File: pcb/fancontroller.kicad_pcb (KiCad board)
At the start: 2 copper layers, 19 x 41.9 mm, 6 parts, among them J1 Thermo

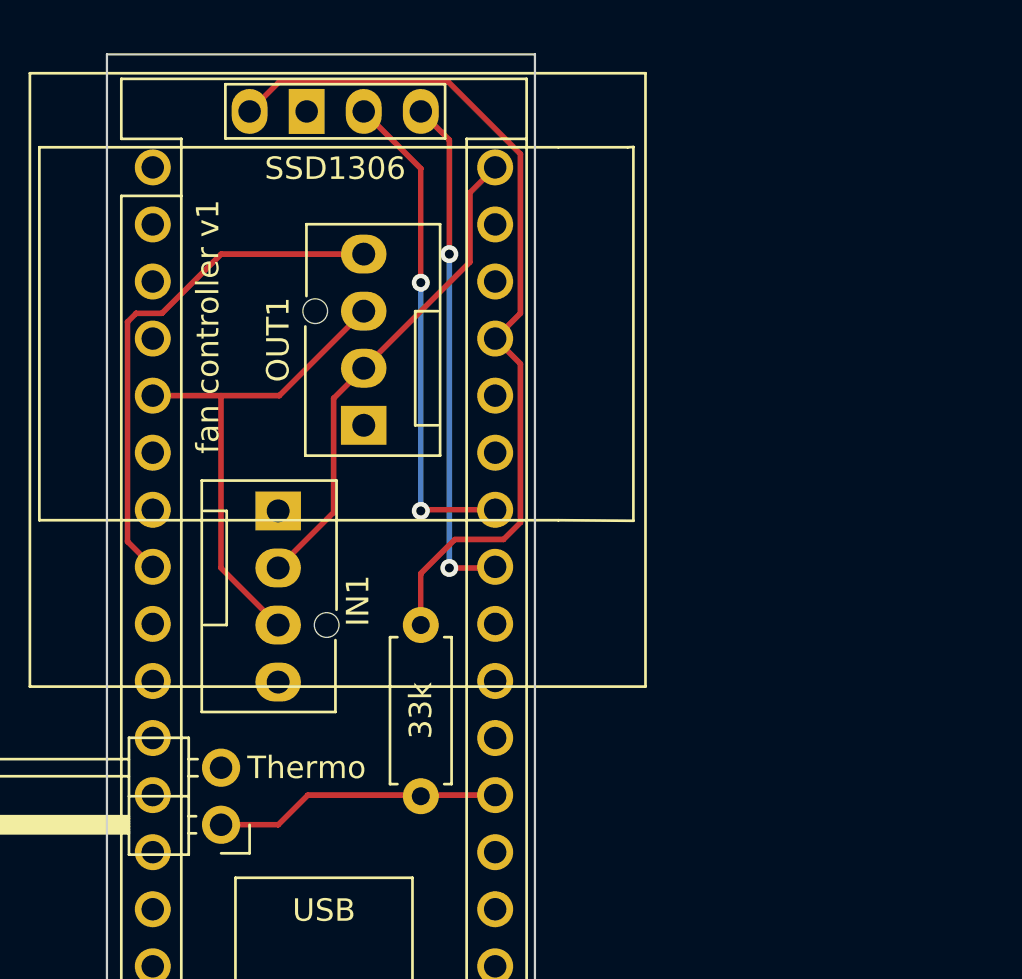
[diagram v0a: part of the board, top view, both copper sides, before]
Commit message: Update to Kicad 8, clean up schematic, add second fan header to schematic
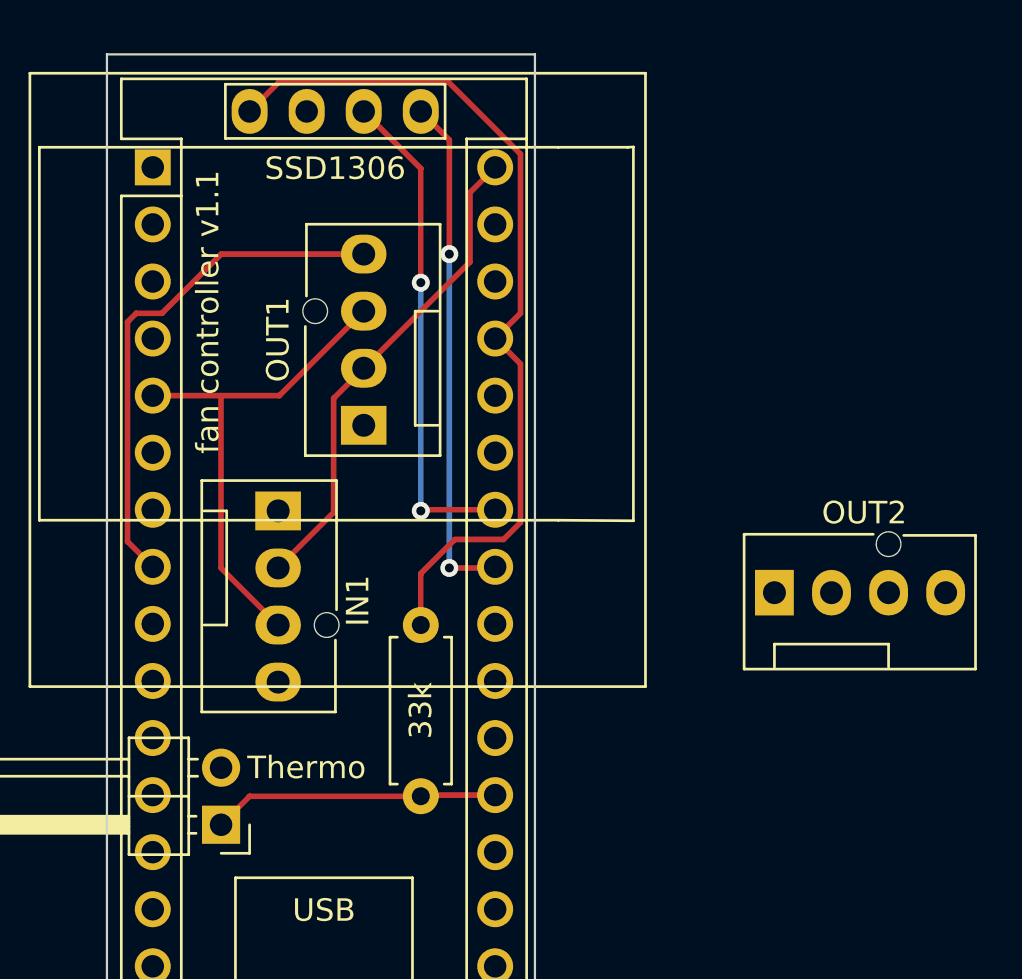
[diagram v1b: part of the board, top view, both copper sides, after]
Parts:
- added OUT2: FAN_HEADER, Connector:FanPinHeader_1x04_P2.54mm_Vertical, F.Cu at (119.9, 90.0)
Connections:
- net Net-(A1-+5V) renamed +5V
- net Net-(A1-A0) renamed /TEMP
- net Net-(A1-A4) renamed /SDA
- net Net-(A1-A5) renamed /SCL
- net Net-(A1-D2) renamed /TACH1
- net Net-(A1-D5) renamed /PWM
- A1 pad 6: unconnected-(A1-D3-Pad6) -> /TACH2
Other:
- board text added: "fan controller v1.1"
- board text removed: "fan controller v1"

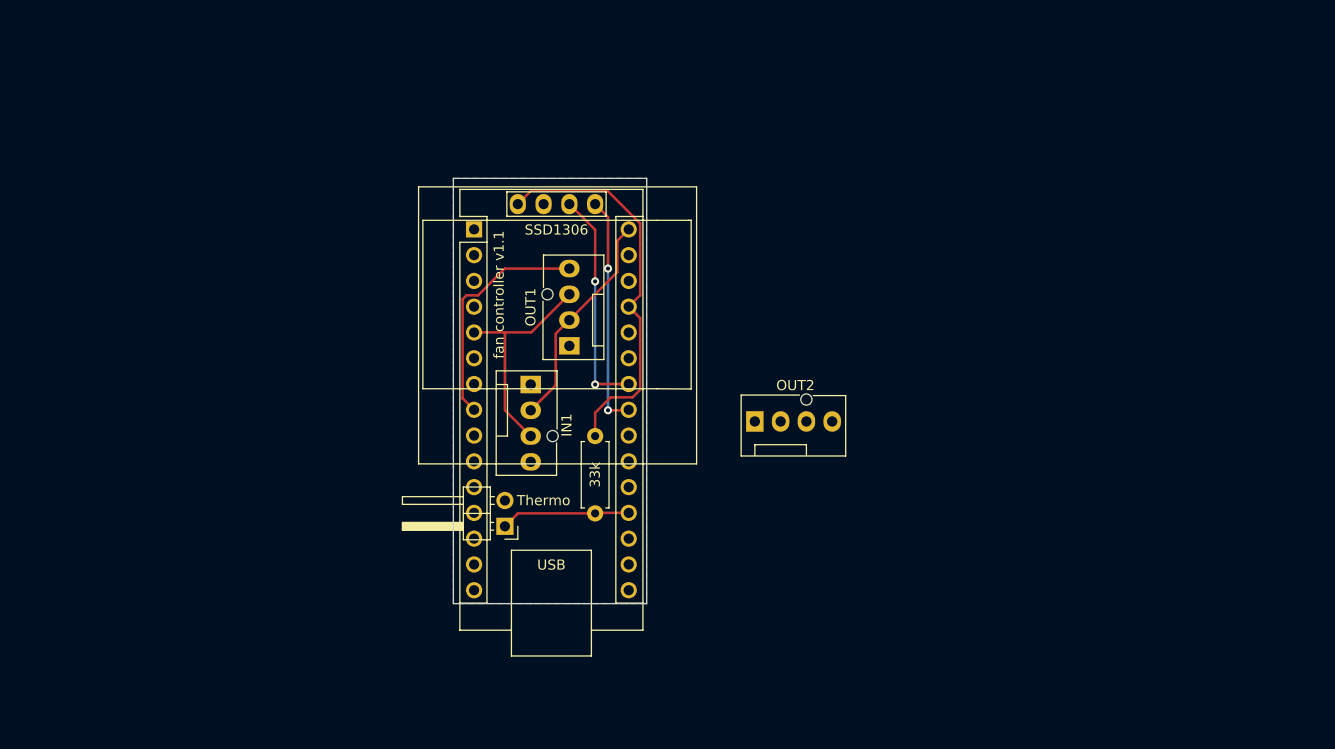
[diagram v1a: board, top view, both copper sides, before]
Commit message: v2: add stm32cubemx config, early draft of pcb layout, update version
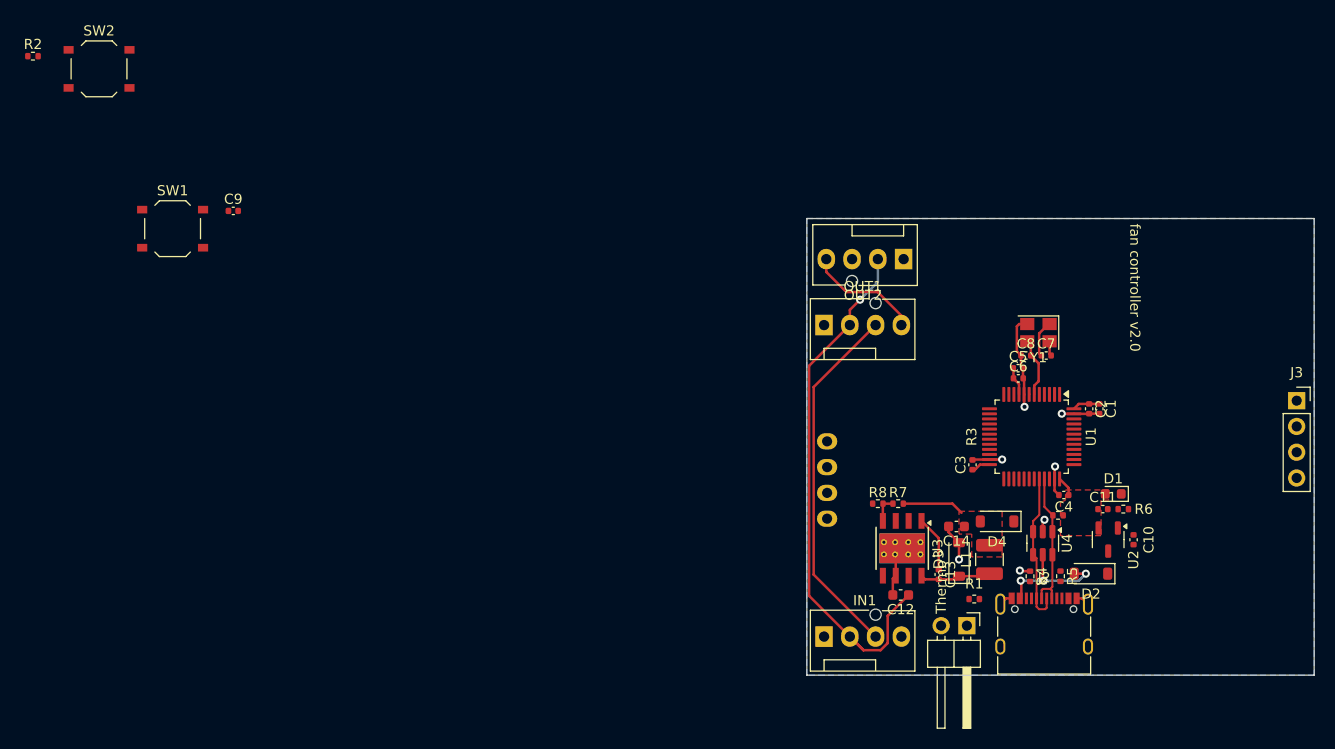
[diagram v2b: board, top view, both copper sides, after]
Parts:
- removed A1: Arduino_Nano_v3.x, Module:Arduino_Nano
- added C1: 4.7uF, Capacitor_SMD:C_0402_1005Metric, F.Cu at (153.8, 88.8)
- added C10: 1uF, Capacitor_SMD:C_0402_1005Metric, F.Cu at (157.2, 101.7)
- added C11: 1uF, Capacitor_SMD:C_0402_1005Metric, F.Cu at (154.2, 98.6)
- added C12: 10uF, Capacitor_SMD:C_0603_1608Metric, F.Cu at (134.2, 107.1)
- added C13: 10nF, Capacitor_SMD:C_0402_1005Metric, F.Cu at (138.0, 105.1)
- added C14: 22uF, Capacitor_SMD:C_0603_1608Metric, F.Cu at (139.8, 100.3)
- added C2: 100nF, Capacitor_SMD:C_0402_1005Metric, F.Cu at (152.8, 88.8)
- added C3: 100nF, Capacitor_SMD:C_0402_1005Metric, F.Cu at (141.3, 94.3)
- added C4: 100nF, Capacitor_SMD:C_0402_1005Metric, F.Cu at (150.3, 97.2)
- added C5: 1uF, Capacitor_SMD:C_0402_1005Metric, F.Cu at (145.8, 84.8)
- added C6: 10nF, Capacitor_SMD:C_0402_1005Metric, F.Cu at (145.8, 85.8)
- added C7: 10pF, Capacitor_SMD:C_0402_1005Metric, F.Cu at (148.6, 83.5)
- added C8: 10pF, Capacitor_SMD:C_0402_1005Metric, F.Cu at (146.6, 83.5)
- added C9: 100n, Capacitor_SMD:C_0402_1005Metric, F.Cu at (68.5, 69.2)
- added D1: white, LED_SMD:LED_0603_1608Metric, F.Cu at (155.2, 97.1)
- added D2: B5819W, Diode_SMD:D_SOD-123, F.Cu at (153.0, 105.0)
- added D3: B5819W, Diode_SMD:D_SOD-123, F.Cu at (140.0, 103.6)
- added D4: B5819W, Diode_SMD:D_SOD-123, F.Cu at (143.8, 99.8)
- added J2: USB_C_PC, Connector_USB:USB_C_Receptacle_XKB_U262-16XN-4BVC11, F.Cu at (148.4, 111.1)
- added J3: SWD, Connector_PinSocket_2.54mm:PinSocket_1x04_P2.54mm_Vertical, F.Cu at (173.3, 88.0)
- added L1: 10uH, Inductor_SMD:L_1210_3225Metric, F.Cu at (143.0, 103.6)
- added R2: 5.1kΩ, Resistor_SMD:R_0402_1005Metric, F.Cu at (48.7, 54.0)
- added R3: 1.5kΩ, Resistor_SMD:R_0402_1005Metric, F.Cu at (149.8, 99.2)
- added R4: 5.1kΩ, Resistor_SMD:R_0402_1005Metric, F.Cu at (147.0, 105.3)
- added R5: 5.1kΩ, Resistor_SMD:R_0402_1005Metric, F.Cu at (150.0, 105.2)
- added R6: 1.5kΩ, Resistor_SMD:R_0402_1005Metric, F.Cu at (156.2, 98.6)
- added R7: 10kΩ, Resistor_SMD:R_0402_1005Metric, F.Cu at (134.0, 98.1)
- added R8: 3.3kΩ, Resistor_SMD:R_0402_1005Metric, F.Cu at (132.0, 98.1)
- added SW1: NRST, Button_Switch_SMD:SW_Push_1P1T_XKB_TS-1187A, F.Cu at (62.5, 71.0)
- added SW2: BOOT0, Button_Switch_SMD:SW_Push_1P1T_XKB_TS-1187A, F.Cu at (55.2, 55.2)
- added U1: STM32F103C8Tx, Package_QFP:LQFP-48_7x7mm_P0.5mm, F.Cu at (147.2, 91.5)
- added U2: XC6206PxxxMR, Package_TO_SOT_SMD:SOT-23-3, F.Cu at (154.7, 101.6)
- added U3: TPS5430DDA, Package_SO:TI_SO-PowerPAD-8_ThermalVias, F.Cu at (134.4, 102.5)
- added U4: USBLC6-2SC6, Package_TO_SOT_SMD:SOT-23-6, F.Cu at (148.2, 102.0)
- added Y1: 16MHz, Crystal:Crystal_SMD_3225-4Pin_3.2x2.5mm, F.Cu at (147.8, 81.2)
- R1: value 33k -> 33kΩ; footprint Resistor_THT:R_Axial_DIN0207_L6.3mm_D2.5mm_P7.62mm_Horizontal -> Resistor_SMD:R_0402_1005Metric
- SSD1306: moved to B.Cu
- moved J1 46.6 mm to (140.8, 110.1), turned to -90 degrees
- moved SSD1306 40.9 mm to (137.6, 95.6), turned to -90 degrees
- moved R1 40.7 mm to (141.5, 107.5), turned to 180 degrees
- moved IN1 38.1 mm to (126.7, 111.2), turned to 0 degrees
- moved OUT1 25.2 mm to (126.7, 80.5), turned to 0 degrees
- moved OUT2 21.7 mm to (134.5, 74.0), turned to 180 degrees
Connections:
- net +5V renamed +3.3V
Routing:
- net GND: track 0.00 -> 33.8 mm, vias 0 -> 7
- net +12V: track 21.8 -> 53.7 mm, vias 0 -> 1
- net +3.3V: track 38.9 -> 9.36 mm
- net /SDA: track 22.8 -> 0.00 mm, vias 2 -> 0
- net /SCL: track 22.2 -> 0.00 mm, vias 2 -> 0
- net /USB_D-: track 0.00 -> 15.1 mm
- net /USB_D+: track 0.00 -> 14.0 mm
- net /TACH1: track 22.2 -> 35.8 mm
- net /TEMP: track 12.7 -> 0.00 mm
- net /VBUS: track 0.00 -> 12.2 mm, vias 0 -> 3
- net /PWM: track 23.1 -> 11.4 mm
- net Net-(D3-K): track 0.00 -> 7.08 mm
- net Net-(D4-A): track 0.00 -> 6.11 mm
- net Net-(U1-PD1): track 0.00 -> 5.88 mm
- net Net-(U3-BOOT): track 0.00 -> 5.50 mm
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- added copper zone on F.Cu, net +3.3V
- added copper zone on F.Cu, net Net-(D4-A)
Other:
- board size 19 x 41.9 mm -> 50 x 45 mm
- board text added: "fan controller v2.0"
- board text removed: "fan controller v1.1"

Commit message: Finish routing assuming OLED module
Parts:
- moved R2 97.3 mm to (141.5, 83.5), turned to 180 degrees
- moved SW2 93.1 mm to (145.0, 80.0)
- moved SW1 82.5 mm to (145.0, 73.5)
- moved C9 72.2 mm to (140.5, 75.0), turned to -90 degrees
- moved J3 27.7 mm to (150.8, 71.8)
- moved R1 19.5 mm to (131.5, 90.8), turned to 0 degrees
- moved C11 11.7 mm to (148.1, 88.7)
- moved D1 11.7 mm to (149.1, 87.2)
- moved R6 11.7 mm to (150.1, 88.7)
- moved U2 11.7 mm to (148.6, 91.7)
- moved C10 11.7 mm to (151.1, 91.7)
- moved C6 9.39 mm to (136.5, 84.5)
- moved C5 9.39 mm to (136.5, 83.5)
- moved C7 8.91 mm to (139.7, 82.5)
- moved C8 8.91 mm to (137.7, 82.5)
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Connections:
- U1 pad 11: /TEMP -> unconnected-(U1-PA1-Pad11)
- U1 pad 12: unconnected-(U1-PA2-Pad12) -> /TACH2
- U1 pad 13: unconnected-(U1-PA3-Pad13) -> /PWM
- U1 pad 14: unconnected-(U1-PA4-Pad14) -> /TACH1
- U1 pad 19: unconnected-(U1-PB1-Pad19) -> /TEMP
- U1 pad 25: /TACH1 -> unconnected-(U1-PB12-Pad25)
- U1 pad 26: /TACH2 -> unconnected-(U1-PB13-Pad26)
- U1 pad 28: /PWM -> unconnected-(U1-PB15-Pad28)
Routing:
- net +3.3V: track 9.36 -> 87.5 mm, vias 0 -> 6
- net /SWDIO: track 0.00 -> 31.6 mm, vias 0 -> 2
- net /SWCLK: track 0.00 -> 31.5 mm
- net /TEMP: track 0.00 -> 29.8 mm, vias 0 -> 4
- net +5V: track 0.00 -> 22.7 mm, vias 0 -> 4
- net /NRST: track 0.02 -> 22.6 mm, vias 0 -> 2
- net /SDA: track 0.00 -> 20.2 mm, vias 0 -> 2
- net /SCL: track 0.00 -> 18.1 mm
- net GND: track 33.8 -> 51.5 mm, vias 7 -> 11
- net /BOOT0: track 0.00 -> 15.7 mm, vias 0 -> 2
- net /TACH2: track 0.00 -> 14.9 mm
- net /USB_D+: track 14.0 -> 22.7 mm
- net /USB_D-: track 15.1 -> 23.3 mm
- net /PWM: track 11.4 -> 18.8 mm
- net Net-(U1-PD0): track 3.67 -> 7.70 mm
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- added copper zone on F.Cu, net +5V
- added copper zone on F.Cu, net GND
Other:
- board size 50 x 45 mm -> 30 x 45 mm

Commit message: Add LED
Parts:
- added D5: white, LED_SMD:LED_0603_1608Metric, F.Cu at (136.2, 96.8)
- added R9: 1.5kΩ, Resistor_SMD:R_0402_1005Metric, F.Cu at (133.5, 96.8)
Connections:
- U1 pad 28: unconnected-(U1-PB15-Pad28) -> Net-(D5-A)
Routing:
- net Net-(D5-A): track 0.00 -> 2.07 mm
- net GND: track 51.5 -> 53.6 mm
- net /APP_LED: track 0.00 -> 1.43 mm
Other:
- board text added: "JLCJLCJLCJLC"

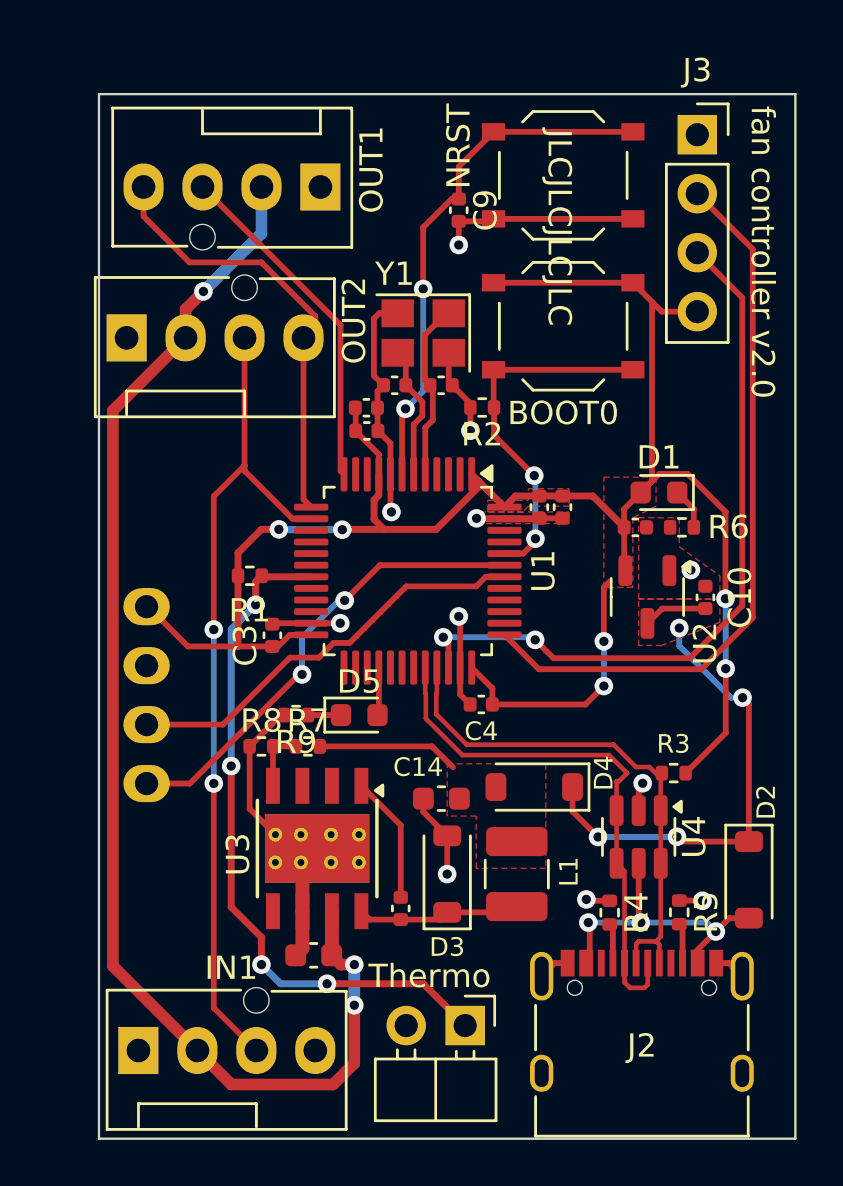
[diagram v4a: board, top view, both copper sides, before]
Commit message: Begin rev3: drop USB connector, plan for OLED mounting
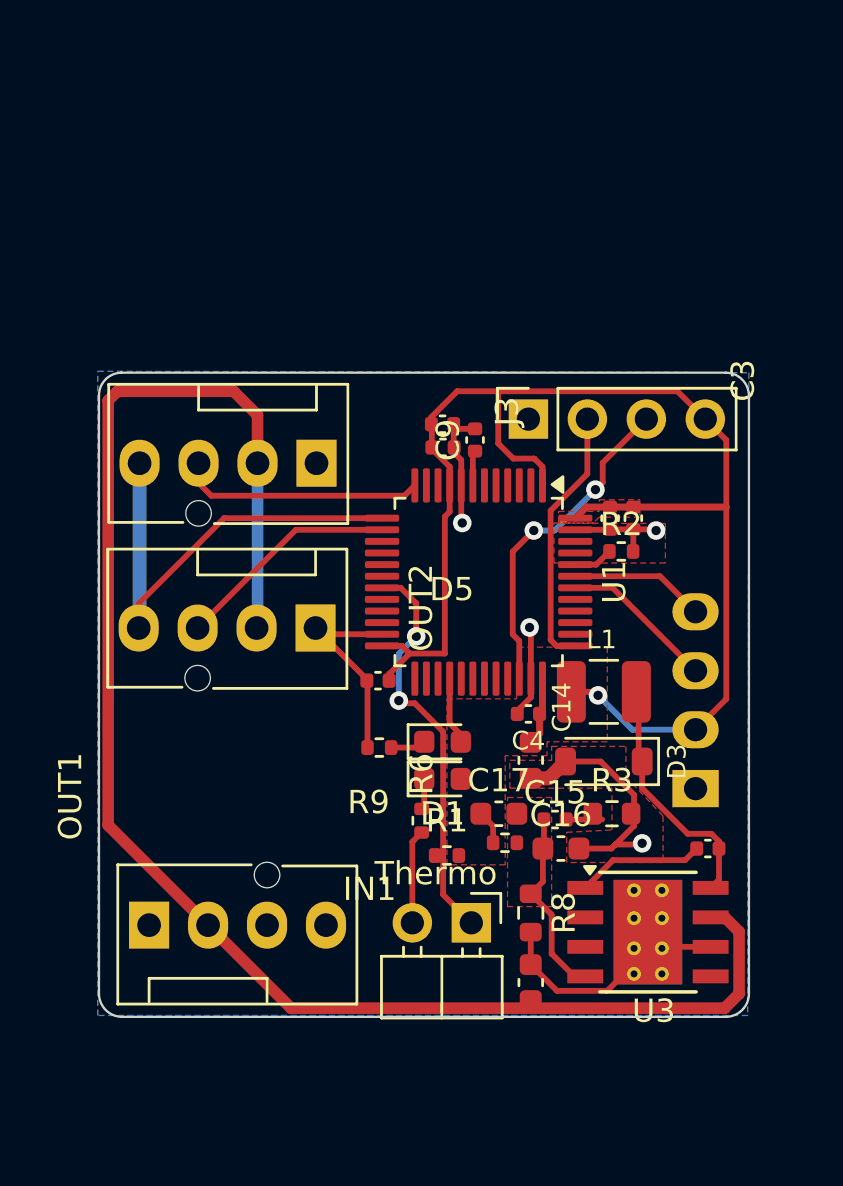
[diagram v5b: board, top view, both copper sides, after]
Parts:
- removed C10, C11: 1uF, Capacitor_SMD:C_0402_1005Metric
- removed C7, C8: 10pF, Capacitor_SMD:C_0402_1005Metric
- removed D2, D4: B5819W, Diode_SMD:D_SOD-123
- removed J2: USB_C_PC, Connector_USB:USB_C_Receptacle_XKB_U262-16XN-4BVC11
- removed R4, R5: 5.1kΩ, Resistor_SMD:R_0402_1005Metric
- removed SW1: NRST, Button_Switch_SMD:SW_Push_1P1T_XKB_TS-1187A
- removed SW2: BOOT0, Button_Switch_SMD:SW_Push_1P1T_XKB_TS-1187A
- removed U2: XC6206PxxxMR, Package_TO_SOT_SMD:SOT-23-3
- removed U4: USBLC6-2SC6, Package_TO_SOT_SMD:SOT-23-6
- removed Y1: 16MHz, Crystal:Crystal_SMD_3225-4Pin_3.2x2.5mm
- added C15: 100nF, Capacitor_SMD:C_0402_1005Metric, F.Cu at (144.7, 101.2)
- added C16: 150pF, Capacitor_SMD:C_0603_1608Metric, F.Cu at (144.9, 102.5)
- added C17: 1.5nF, Capacitor_SMD:C_0603_1608Metric, F.Cu at (142.2, 101.0)
- R3: value 1.5kΩ -> 549Ω; footprint Resistor_SMD:R_0402_1005Metric -> Resistor_SMD:R_0603_1608Metric
- R8: value 3.3kΩ -> 5.9kΩ; footprint Resistor_SMD:R_0402_1005Metric -> Resistor_SMD:R_0603_1608Metric
- moved R6 16.9 mm to (138.9, 101.3), turned to -90 degrees
- moved D1 15.5 mm to (139.8, 99.5), turned to 0 degrees
- moved OUT1 14.9 mm to (134.3, 93.0), turned to 180 degrees
- moved R1 14.7 mm to (140.0, 102.8), turned to 180 degrees
- moved U3 14.7 mm to (148.7, 106.1), turned to 0 degrees
- moved J3 14.2 mm to (143.5, 84.0), turned to 90 degrees
- moved R8 13.6 mm to (143.6, 105.3), turned to -90 degrees
- moved C13 13.5 mm to (151.2, 102.5), turned to 0 degrees
- moved OUT2 11.9 mm to (134.4, 85.9)
- moved C9 9.92 mm to (141.2, 84.9), turned to 90 degrees
- moved R7 9.45 mm to (142.5, 102.2), turned to 0 degrees
- moved C12 9.42 mm to (143.6, 108.3), turned to 90 degrees
- moved L1 8.70 mm to (146.8, 95.8), turned to 180 degrees
- moved R2 8.62 mm to (147.5, 89.7), turned to 0 degrees
- moved D3 8.31 mm to (146.8, 98.8), turned to 180 degrees
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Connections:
- net Net-(U3-VSENSE) renamed /PFSENSE
- C14 pad 1: Net-(D4-A) -> +3.3V
- L1 pad 2: Net-(D4-A) -> +3.3V
- R3 pad 1: /USB_D+ -> Net-(C15-Pad2)
- R3 pad 2: +3.3V -> GND
- R7 pad 1: Net-(D4-A) -> +3.3V
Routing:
- net /TACH1: track 36.0 -> 9.70 mm, vias 2 -> 0
- net /USB_D-: track 23.3 -> 0.00 mm
- net +3.3V: track 87.5 -> 64.5 mm, vias 6 -> 1
- net +5V: track 22.7 -> 0.00 mm, vias 4 -> 0
- net /USB_D+: track 22.7 -> 0.00 mm
- net /NRST: track 22.6 -> 1.51 mm, vias 2 -> 0
- net /SWCLK: track 31.5 -> 11.3 mm
- net /SWDIO: track 31.6 -> 14.2 mm
- net /SDA: track 20.2 -> 5.82 mm, vias 2 -> 0
- net /BOOT0: track 15.7 -> 1.71 mm, vias 2 -> 0
- net /VBUS: track 13.4 -> 0.00 mm, vias 3 -> 0
- net +12V: track 56.4 -> 69.4 mm, vias 3 -> 0
- net /TEMP: track 29.8 -> 17.5 mm, vias 4 -> 2
- net /SCL: track 18.1 -> 6.66 mm
- net Net-(U1-PD0): track 7.70 -> 0.00 mm
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- added copper zone on F.Cu, net /PFSENSE
- removed copper zone on F.Cu, net +5V
- removed copper zone on F.Cu, net Net-(D4-A)
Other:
- board size 30 x 45 mm -> 28 x 27.8 mm
- board text added: "fan controller v3.0"
- board text removed: "JLCJLCJLCJLC"
- board text removed: "fan controller v2.0"
